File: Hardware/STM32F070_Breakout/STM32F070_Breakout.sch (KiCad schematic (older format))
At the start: 34 parts, among them J1 USB_B_Micro, J2 Conn_01x16, J3 Conn_01x16, J4 Conn_01x05, SW1 SW_Push, SW2 SW_Push, U1 AP2112K-3.3, U2 STM32F070CBT6, Y1 32.768kHZ, Y2 16MHz

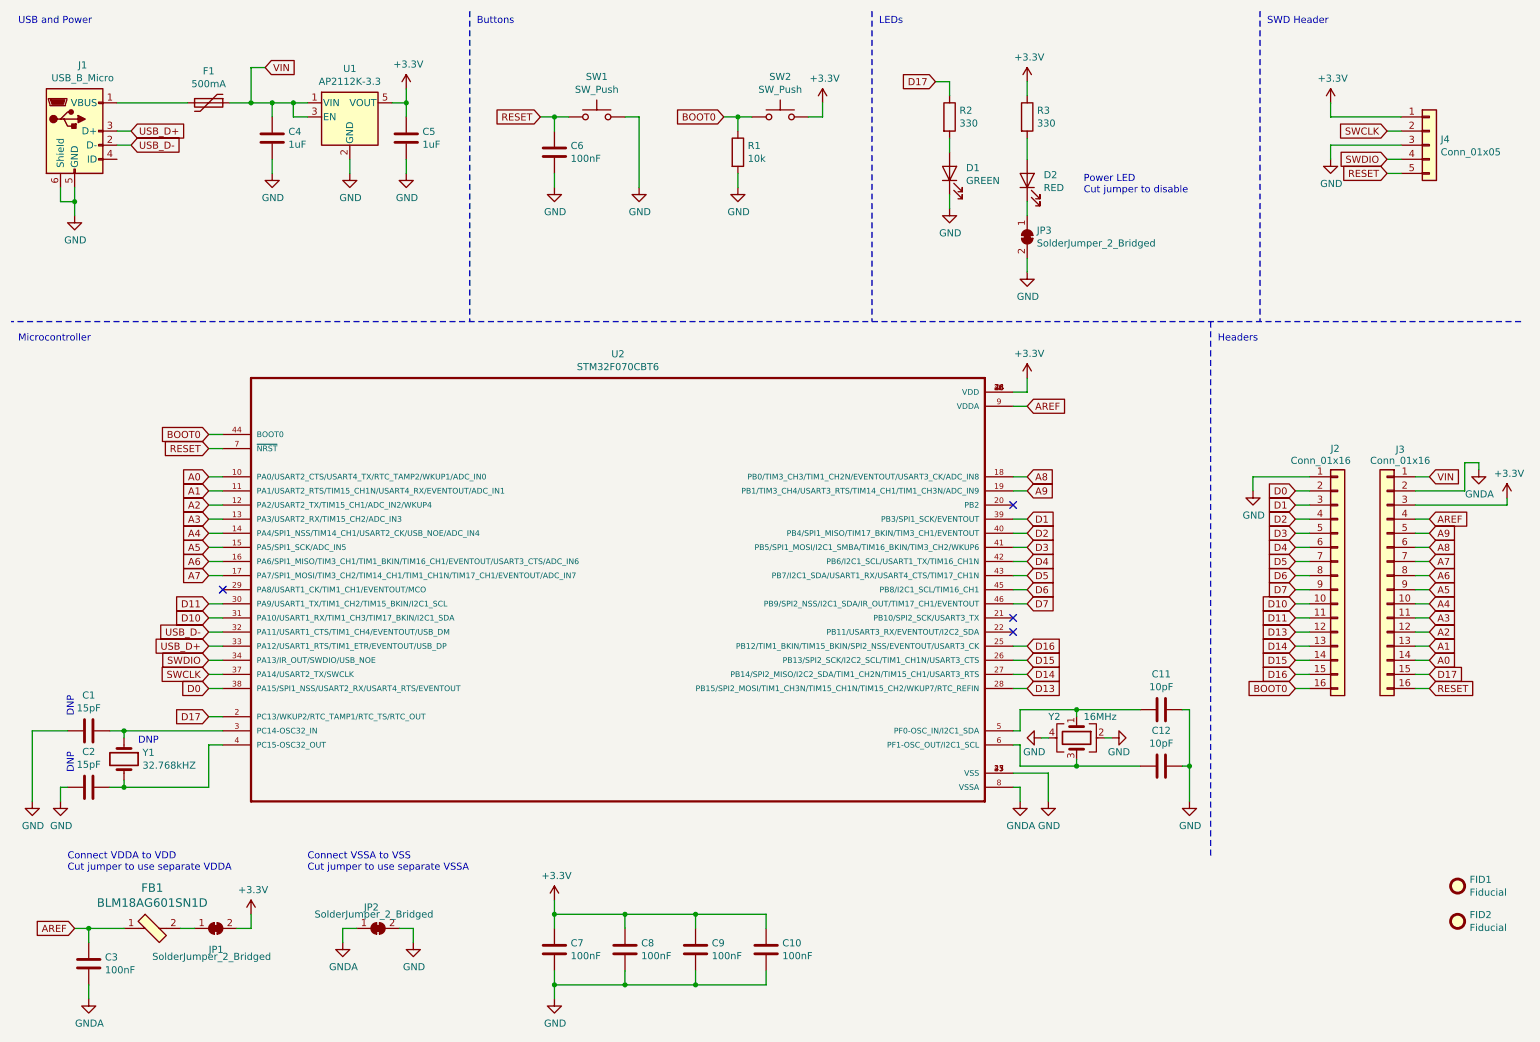
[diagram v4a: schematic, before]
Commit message: Version v01 complete and sent for fab.
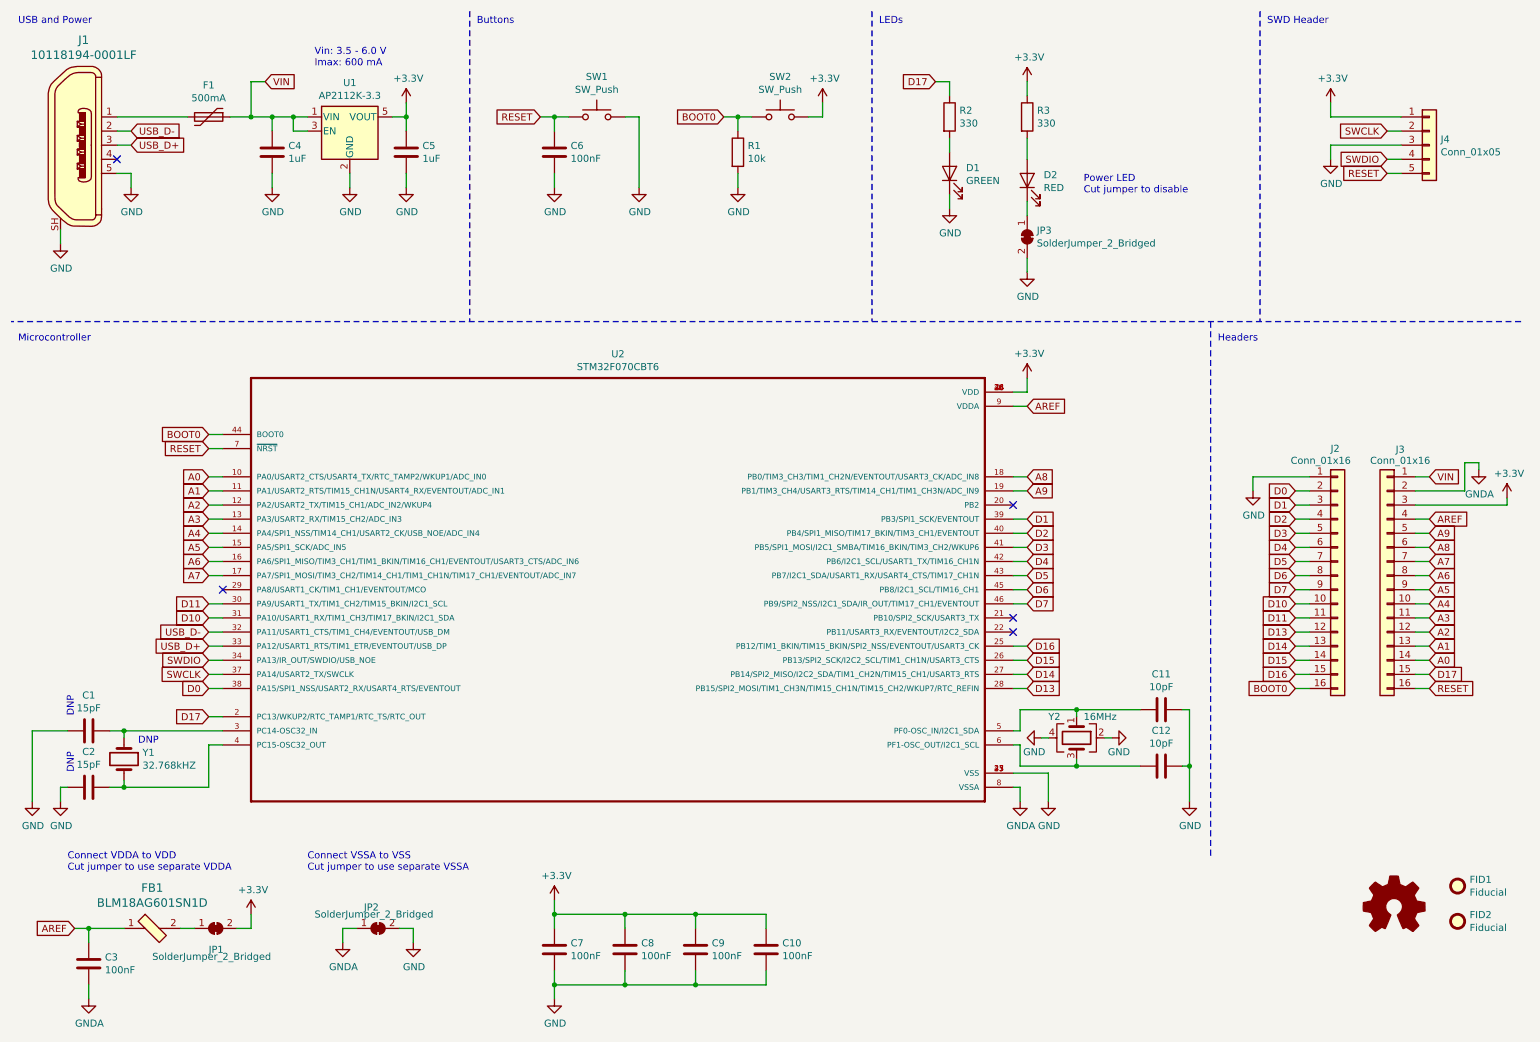
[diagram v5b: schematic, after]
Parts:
- removed J1: USB_B_Micro, digikey-footprints:USB_Micro_B_Female_10118194-0001LF, symbol Connector:USB_B_Micro
- added J1: 10118194-0001LF, digikey-footprints:USB_Micro_B_Female_10118194-0001LF, symbol dk_USB-DVI-HDMI-Connectors:10118194-0001LF
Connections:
- net GND: now also J1.5, J1.SH
- net USB_D+: now also J1.3
- net USB_D-: now also J1.2
- net at F1.2: now also J1.1
- no-connect marks 4 -> 5
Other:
- note added: "Vin: 3.5 - 6.0 V\nImax: 600 mA"
- moved on the sheet: C4, C5, F1, U1
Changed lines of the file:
@@
 $EndDescr
-$Comp
-L Connector:USB_B_Micro J1
-U 1 1 5CF022E5
-P 950 1350
-F 0 "J1" H 1007 1817 50  0000 C CNN
-F 1 "USB_B_Micro" H 1007 1726 50  0000 C CNN
-F 2 "digikey-footprints:USB_Micro_B_Female_10118194-0001LF" H 1100 1300 50  0001 C CNN
-F 3 "~" H 1100 1300 50  0001 C CNN
-	1    950  1350
-	1    0    0    -1
-$EndComp
 $Comp
 L Device:Polyfuse F1
 U 1 1 5CF03193
-P 1900 1150
-F 0 "F1" V 1675 1150 50  0000 C CNN
-F 1 "500mA" V 1766 1150 50  0000 C CNN
-F 2 "footprints:0ZCK0050FF2E" H 1950 950 50  0001 L CNN
-F 3 "~" H 1900 1150 50  0001 C CNN
-	1    1900 1150
+P 1900 1250
+F 0 "F1" V 1675 1250 50  0000 C CNN
+F 1 "500mA" V 1766 1250 50  0000 C CNN
+F 2 "footprints:0ZCK0050FF2E" H 1950 1050 50  0001 L CNN
+F 3 "~" H 1900 1250 50  0001 C CNN
+	1    1900 1250
 	0    1    1    0
 $EndComp
@@
 L Regulator_Linear:AP2112K-3.3 U1
 U 1 1 5CF03C56
-P 2900 1250
-F 0 "U1" H 2900 1592 50  0000 C CNN
-F 1 "AP2112K-3.3" H 2900 1501 50  0000 C CNN
-F 2 "Package_TO_SOT_SMD:SOT-23-5" H 2900 1575 50  0001 C CNN
-F 3 "https://www.diodes.com/assets/Datasheets/AP2112.pdf" H 2900 1350 50  0001 C CNN
-	1    2900 1250
+P 2900 1350
+F 0 "U1" H 2900 1692 50  0000 C CNN
+F 1 "AP2112K-3.3" H 2900 1601 50  0000 C CNN
+F 2 "Package_TO_SOT_SMD:SOT-23-5" H 2900 1675 50  0001 C CNN
+F 3 "https://www.diodes.com/assets/Datasheets/AP2112.pdf" H 2900 1450 50  0001 C CNN
+	1    2900 1350
 	1    0    0    -1
 $EndComp
@@
 L Device:C C4
 U 1 1 5CF04C4A
-P 2350 1400
-F 0 "C4" H 2465 1446 50  0000 L CNN
-F 1 "1uF" H 2465 1355 50  0000 L CNN
-F 2 "Capacitor_SMD:C_0603_1608Metric" H 2388 1250 50  0001 C CNN
-F 3 "~" H 2350 1400 50  0001 C CNN
-	1    2350 1400
+P 2350 1500
+F 0 "C4" H 2465 1546 50  0000 L CNN
+F 1 "1uF" H 2465 1455 50  0000 L CNN
+F 2 "Capacitor_SMD:C_0603_1608Metric" H 2388 1350 50  0001 C CNN
+F 3 "~" H 2350 1500 50  0001 C CNN
+	1    2350 1500
 	1    0    0    -1
 $EndComp
@@
 L Device:C C5
 U 1 1 5CF05356
-P 3300 1400
-F 0 "C5" H 3415 1446 50  0000 L CNN
-F 1 "1uF" H 3415 1355 50  0000 L CNN
-F 2 "Capacitor_SMD:C_0603_1608Metric" H 3338 1250 50  0001 C CNN
-F 3 "~" H 3300 1400 50  0001 C CNN
-	1    3300 1400
+P 3300 1500
+F 0 "C5" H 3415 1546 50  0000 L CNN
+F 1 "1uF" H 3415 1455 50  0000 L CNN
+F 2 "Capacitor_SMD:C_0603_1608Metric" H 3338 1350 50  0001 C CNN
+F 3 "~" H 3300 1500 50  0001 C CNN
+	1    3300 1500
 	1    0    0    -1
 $EndComp
@@
 	1    0    0    -1
 $EndComp
-$Comp
-L power:GND #PWR03
-U 1 1 5CF140F9
-P 950 1950
-F 0 "#PWR03" H 950 1700 50  0001 C CNN
-F 1 "GND" H 955 1777 50  0000 C CNN
-F 2 "" H 950 1950 50  0001 C CNN
-F 3 "" H 950 1950 50  0001 C CNN
-	1    950  1950
-	1    0    0    -1
-$EndComp
-Wire Wire Line
-	850  1750 850  1850
-Wire Wire Line
-	850  1850 950  1850
-Wire Wire Line
-	950  1850 950  1750
-Wire Wire Line
-	950  1850 950  1950
-Connection ~ 950  1850
-Wire Wire Line
-	1250 1350 1350 1350
-Wire Wire Line
-	1250 1450 1350 1450
+Text GLabel 1350 1450 2    50   Input ~ 0
+USB_D+
 Text GLabel 1350 1350 2    50   Input ~ 0
-USB_D+
-Text GLabel 1350 1450 2    50   Input ~ 0
 USB_D-
 Wire Wire Line
-	1250 1150 1750 1150
-Wire Wire Line
-	2050 1150 2200 1150
-Wire Wire Line
-	2600 1250 2500 1250
-Wire Wire Line
-	2500 1250 2500 1150
-Connection ~ 2500 1150
-Wire Wire Line
-	2500 1150 2600 1150
-Wire Wire Line
-	2350 1150 2350 1250
-Connection ~ 2350 1150
-Wire Wire Line
-	2350 1150 2500 1150
-Wire Wire Line
-	3200 1150 3300 1150
-Wire Wire Line
-	3300 1150 3300 1250
-Wire Wire Line
-	3300 1150 3300 1050
-Connection ~ 3300 1150
+	1250 1250 1750 1250
+Wire Wire Line
+	2050 1250 2200 1250
+Wire Wire Line
+	2600 1350 2500 1350
+Wire Wire Line
+	2500 1350 2500 1250
+Connection ~ 2500 1250
+Wire Wire Line
+	2500 1250 2600 1250
+Wire Wire Line
+	2350 1250 2350 1350
+Connection ~ 2350 1250
+Wire Wire Line
+	2350 1250 2500 1250
+Wire Wire Line
+	3200 1250 3300 1250
+Wire Wire Line
+	3300 1250 3300 1350
+Wire Wire Line
+	3300 1250 3300 1150
+Connection ~ 3300 1250
 $Comp
 L power:GND #PWR06
 U 1 1 5CF1A829
-P 2350 1650
-F 0 "#PWR06" H 2350 1400 50  0001 C CNN
-F 1 "GND" H 2355 1477 50  0000 C CNN
-F 2 "" H 2350 1650 50  0001 C CNN
-F 3 "" H 2350 1650 50  0001 C CNN
-	1    2350 1650
+P 2350 1750
+F 0 "#PWR06" H 2350 1500 50  0001 C CNN
+F 1 "GND" H 2355 1577 50  0000 C CNN
+F 2 "" H 2350 1750 50  0001 C CNN
+F 3 "" H 2350 1750 50  0001 C CNN
+	1    2350 1750
 	1    0    0    -1
 $EndComp
@@
 L power:GND #PWR08
 U 1 1 5CF1B146
-P 2900 1650
-F 0 "#PWR08" H 2900 1400 50  0001 C CNN
-F 1 "GND" H 2905 1477 50  0000 C CNN
-F 2 "" H 2900 1650 50  0001 C CNN
-F 3 "" H 2900 1650 50  0001 C CNN
-	1    2900 1650
+P 2900 1750
+F 0 "#PWR08" H 2900 1500 50  0001 C CNN
+F 1 "GND" H 2905 1577 50  0000 C CNN
+F 2 "" H 2900 1750 50  0001 C CNN
+F 3 "" H 2900 1750 50  0001 C CNN
+	1    2900 1750
 	1    0    0    -1
 $EndComp
@@
 L power:GND #PWR010
 U 1 1 5CF1B368
-P 3300 1650
-F 0 "#PWR010" H 3300 1400 50  0001 C CNN
-F 1 "GND" H 3305 1477 50  0000 C CNN
-F 2 "" H 3300 1650 50  0001 C CNN
-F 3 "" H 3300 1650 50  0001 C CNN
-	1    3300 1650
-	1    0    0    -1
-$EndComp
-Wire Wire Line
-	2350 1550 2350 1650
-Wire Wire Line
-	2900 1550 2900 1650
-Wire Wire Line
-	3300 1550 3300 1650
+P 3300 1750
+F 0 "#PWR010" H 3300 1500 50  0001 C CNN
+F 1 "GND" H 3305 1577 50  0000 C CNN
+F 2 "" H 3300 1750 50  0001 C CNN
+F 3 "" H 3300 1750 50  0001 C CNN
+	1    3300 1750
+	1    0    0    -1
+$EndComp
+Wire Wire Line
+	2350 1650 2350 1750
+Wire Wire Line
+	2900 1650 2900 1750
+Wire Wire Line
+	3300 1650 3300 1750
 $Comp
 L power:+3.3V #PWR09
 U 1 1 5CF1C2BF
-P 3300 1050
-F 0 "#PWR09" H 3300 900 50  0001 C CNN
-F 1 "+3.3V" H 3315 1223 50  0000 C CNN
-F 2 "" H 3300 1050 50  0001 C CNN
-F 3 "" H 3300 1050 50  0001 C CNN
-	1    3300 1050
-	1    0    0    -1
-$EndComp
-Wire Wire Line
-	2200 1150 2200 900
-Wire Wire Line
-	2200 900  2300 900
-Connection ~ 2200 1150
-Wire Wire Line
-	2200 1150 2350 1150
-Text GLabel 2300 900  2    50   Input ~ 0
+P 3300 1150
+F 0 "#PWR09" H 3300 1000 50  0001 C CNN
+F 1 "+3.3V" H 3315 1323 50  0000 C CNN
+F 2 "" H 3300 1150 50  0001 C CNN
+F 3 "" H 3300 1150 50  0001 C CNN
+	1    3300 1150
+	1    0    0    -1
+$EndComp
+Wire Wire Line
+	2200 1250 2200 1000
+Wire Wire Line
+	2200 1000 2300 1000
+Connection ~ 2200 1250
+Wire Wire Line
+	2200 1250 2350 1250
+Text GLabel 2300 1000 2    50   Input ~ 0
 VIN
 $Comp
@@
 Wire Wire Line
 	10450 4200 10550 4200
+$Comp
+L Graphic:Logo_Open_Hardware_Small #LOGO1
+U 1 1 5CFB14F5
+P 10300 6850
+F 0 "#LOGO1" H 10300 7125 50  0001 C CNN
+F 1 "Logo_Open_Hardware_Small" H 10300 6625 50  0001 C CNN
+F 2 "" H 10300 6850 50  0001 C CNN
+F 3 "~" H 10300 6850 50  0001 C CNN
+	1    10300 6850
+	1    0    0    -1
+$EndComp
+$Comp
+L dk_USB-DVI-HDMI-Connectors:10118194-0001LF J1
+U 1 1 5CFB603F
+P 950 1450
+F 0 "J1" H 1014 2195 60  0000 C CNN
+F 1 "10118194-0001LF" H 1014 2089 60  0000 C CNN
+F 2 "digikey-footprints:USB_Micro_B_Female_10118194-0001LF" H 1150 1650 60  0001 L CNN
+F 3 "http://www.amphenol-icc.com/media/wysiwyg/files/drawing/10118194.pdf" H 1150 1750 60  0001 L CNN
+F 4 "609-4618-1-ND" H 1150 1850 60  0001 L CNN "Digi-Key_PN"
+F 5 "10118194-0001LF" H 1150 1950 60  0001 L CNN "MPN"
+F 6 "Connectors, Interconnects" H 1150 2050 60  0001 L CNN "Category"
+F 7 "USB, DVI, HDMI Connectors" H 1150 2150 60  0001 L CNN "Family"
+F 8 "http://www.amphenol-icc.com/media/wysiwyg/files/drawing/10118194.pdf" H 1150 2250 60  0001 L CNN "DK_Datasheet_Link"
+F 9 "/product-detail/en/amphenol-icc-fci/10118194-0001LF/609-4618-1-ND/2785382" H 1150 2350 60  0001 L CNN "DK_Detail_Page"
+F 10 "CONN RCPT USB2.0 MICRO B SMD R/A" H 1150 2450 60  0001 L CNN "Description"
+F 11 "Amphenol ICC (FCI)" H 1150 2550 60  0001 L CNN "Manufacturer"
+F 12 "Active" H 1150 2650 60  0001 L CNN "Status"
+	1    950  1450
+	1    0    0    -1
+$EndComp
+$Comp
+L power:GND #PWR03
+U 1 1 5CF140F9
+P 850 2150
+F 0 "#PWR03" H 850 1900 50  0001 C CNN
+F 1 "GND" H 855 1977 50  0000 C CNN
+F 2 "" H 850 2150 50  0001 C CNN
+F 3 "" H 850 2150 50  0001 C CNN
+	1    850  2150
+	1    0    0    -1
+$EndComp
+$Comp
+L power:GND #PWR0105
+U 1 1 5CFB92F0
+P 1350 1750
+F 0 "#PWR0105" H 1350 1500 50  0001 C CNN
+F 1 "GND" H 1355 1577 50  0000 C CNN
+F 2 "" H 1350 1750 50  0001 C CNN
+F 3 "" H 1350 1750 50  0001 C CNN
+	1    1350 1750
+	1    0    0    -1
+$EndComp
+Wire Wire Line
+	1250 1350 1350 1350
+Wire Wire Line
+	1250 1450 1350 1450
+Wire Wire Line
+	1250 1650 1350 1650
+Wire Wire Line
+	1350 1650 1350 1750
+Wire Wire Line
+	850  2050 850  2150
+NoConn ~ 1250 1550
+Text Notes 2650 900  0    50   ~ 0
+Vin: 3.5 - 6.0 V\nImax: 600 mA
 $EndSCHEMATC

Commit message: Finished v02 layout
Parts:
- added J5, J6, J7: Conn_01x01, STM32F070_Breakout:TestPoint_Pad_1.0x2.5mm, symbol Connector_Generic:Conn_01x01
- FB1: footprint digikey-footprints:0603 -> Resistor_SMD:R_0603_1608Metric
- R2, R3: value 330 -> 1k
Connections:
- net D30: now reaches U2.21 (PB10/SPI2_SCK/USART3_TX)
- net D30: now also J6.1 (Pin_1)
- net D31: now reaches U2.22 (PB11/USART3_RX/EVENTOUT/I2C2_SDA)
- net D31: now also J7.1 (Pin_1)
- net D12: now reaches U2.29 (PA8/USART1_CK/TIM1_CH1/EVENTOUT/MCO)
- net D12: now also J5.1 (Pin_1)
- net D17 renamed D20
- no-connect marks 5 -> 2
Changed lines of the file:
@@
 encoding utf-8
 Sheet 1 1
-Title "STM32F070 Breakout"
+Title "YAS-0 Board"
 Date "2019-05-30"
-Rev "v01"
+Rev "v02"
 Comp ""
 Comment1 ""
@@
 P 7150 1250
 F 0 "R2" H 7220 1296 50  0000 L CNN
-F 1 "330" H 7220 1205 50  0000 L CNN
+F 1 "1k" H 7220 1205 50  0000 L CNN
 F 2 "Resistor_SMD:R_0603_1608Metric" V 7080 1250 50  0001 C CNN
 F 3 "~" H 7150 1250 50  0001 C CNN
@@
 P 7700 1250
 F 0 "R3" H 7770 1296 50  0000 L CNN
-F 1 "330" H 7770 1205 50  0000 L CNN
+F 1 "1k" H 7770 1205 50  0000 L CNN
 F 2 "Resistor_SMD:R_0603_1608Metric" V 7630 1250 50  0001 C CNN
 F 3 "~" H 7700 1250 50  0001 C CNN
@@
 	7150 1000 7050 1000
 Text GLabel 7050 1000 0    50   Input ~ 0
-D17
+D20
 $Comp
 L Connector_Generic:Conn_01x05 J4
@@
 Text GLabel 1900 4500 0    50   Input ~ 0
 A7
-NoConn ~ 2000 4600
 Text GLabel 1900 4700 0    50   Input ~ 0
 D11
@@
 D0
 Text GLabel 1900 5500 0    50   Input ~ 0
-D17
+D20
 $Comp
 L power:+3.3V #PWR021
@@
 F 0 "FB1" H 1500 7287 60  0000 C CNN
 F 1 "BLM18AG601SN1D" H 1500 7181 60  0000 C CNN
-F 2 "digikey-footprints:0603" H 1700 7200 60  0001 L CNN
+F 2 "Resistor_SMD:R_0603_1608Metric" H 1700 7200 60  0001 L CNN
 F 3 "https://www.murata.com/en-us/products/productdata/8796738650142/ENFA0003.pdf" H 1700 7300 60  0001 L CNN
 F 4 "490-1014-1-ND" H 1700 7400 60  0001 L CNN "Digi-Key_PN"
@@
 Text GLabel 7700 4700 2    50   Input ~ 0
 D7
-NoConn ~ 7600 4800
-NoConn ~ 7600 4900
 Text GLabel 7700 5000 2    50   Input ~ 0
 D16
@@
 	9700 5300 9600 5300
 Text GLabel 10550 5200 2    50   Input ~ 0
-D17
+D20
 Text GLabel 10550 5300 2    50   Input ~ 0
 RESET
@@
 Text Notes 2650 900  0    50   ~ 0
 Vin: 3.5 - 6.0 V\nImax: 600 mA
+Wire Wire Line
+	2000 4600 1900 4600
+Text GLabel 1900 4600 0    50   Input ~ 0
+D12
+$Comp
+L Connector_Generic:Conn_01x01 J5
+U 1 1 5D492255
+P 10400 5750
+F 0 "J5" H 10480 5792 50  0000 L CNN
+F 1 "Conn_01x01" H 10480 5701 50  0000 L CNN
+F 2 "STM32F070_Breakout:TestPoint_Pad_1.0x2.5mm" H 10400 5750 50  0001 C CNN
+F 3 "~" H 10400 5750 50  0001 C CNN
+	1    10400 5750
+	1    0    0    -1
+$EndComp
+$Comp
+L Connector_Generic:Conn_01x01 J6
+U 1 1 5D492A9F
+P 10400 5950
+F 0 "J6" H 10480 5992 50  0000 L CNN
+F 1 "Conn_01x01" H 10480 5901 50  0000 L CNN
+F 2 "STM32F070_Breakout:TestPoint_Pad_1.0x2.5mm" H 10400 5950 50  0001 C CNN
+F 3 "~" H 10400 5950 50  0001 C CNN
+	1    10400 5950
+	1    0    0    -1
+$EndComp
+Wire Wire Line
+	10200 5750 10100 5750
+Wire Wire Line
+	10200 5950 10100 5950
+Text GLabel 10100 5750 0    50   Input ~ 0
+D12
+Wire Wire Line
+	7600 4900 7700 4900
+Text GLabel 7700 4900 2    50   Input ~ 0
+D31
+Text GLabel 10100 5950 0    50   Input ~ 0
+D30
+$Comp
+L Connector_Generic:Conn_01x01 J7
+U 1 1 5D519CA9
+P 10400 6150
+F 0 "J7" H 10480 6192 50  0000 L CNN
+F 1 "Conn_01x01" H 10480 6101 50  0000 L CNN
+F 2 "STM32F070_Breakout:TestPoint_Pad_1.0x2.5mm" H 10400 6150 50  0001 C CNN
+F 3 "~" H 10400 6150 50  0001 C CNN
+	1    10400 6150
+	1    0    0    -1
+$EndComp
+Wire Wire Line
+	10200 6150 10100 6150
+Text GLabel 10100 6150 0    50   Input ~ 0
+D31
+Wire Wire Line
+	7600 4800 7700 4800
+Text GLabel 7700 4800 2    50   Input ~ 0
+D30
 $EndSCHEMATC
